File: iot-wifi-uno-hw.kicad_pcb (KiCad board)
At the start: 2 copper layers, 68.6 x 53.3 mm, 87 parts, among them CON1 BARREL_JACK, P1 CONN_01X08, P2 CONN_01X08, P3 CONN_01X06, P4 CONN_01X10, P5 CONN_01X04, Q1 MMBT8050LT1G, Q2 MMBT8050LT1G, U1 usb_mini_b, U2 MCP16311-MNY, U3 CH340G, U4 ESP-12E, U5 MCP6001R, U6 BD00GA5WEFJ, U7 IRLM6402, X1 CRYSTAL_ABM3C

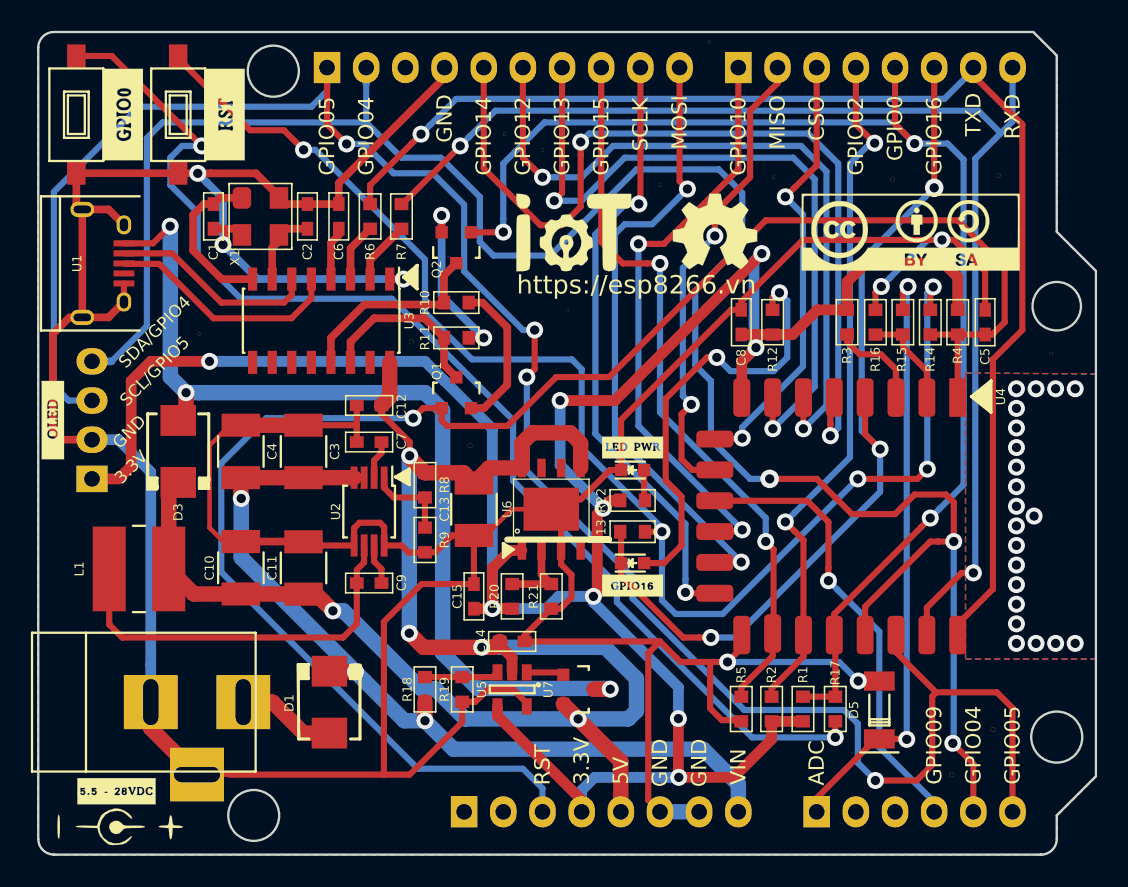
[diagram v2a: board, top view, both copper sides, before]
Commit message: Fix Zone at module wifi esp-12
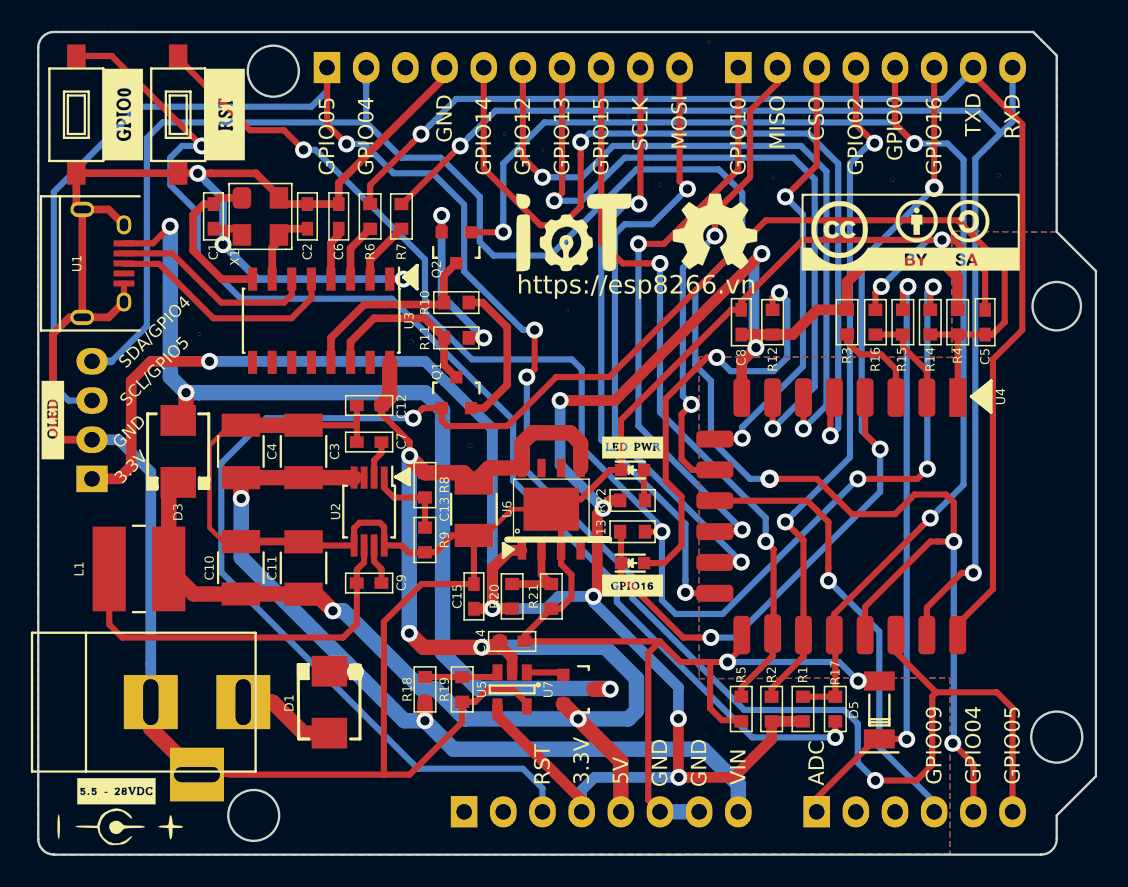
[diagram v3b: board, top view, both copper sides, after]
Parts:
- removed the REF** at (168.2, 106.8)
- removed the REF** at (174.6, 79.5)
- removed the REF** at (170.8, 103.9)
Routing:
- net (no net): vias 21 -> 0
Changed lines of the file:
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@@
   (general
     (links 164)
-    (no_connects 5)
-    (area 107.7265 55.797666 178.201339 114.382333)
+    (no_connects 16)
+    (area 107.7265 55.404 187.068335 114.382333)
     (thickness 1.6)
-    (drawings 87)
-    (tracks 850)
+    (drawings 89)
+    (tracks 829)
     (zones 0)
-    (modules 87)
+    (modules 84)
     (nets 50)
   )
@@
   )
   (module ESP8266:gnd_via (layer F.Cu)
-    (at 174.625 79.502)
-    (fp_text reference REF** (at 0.1016 0.8636) (layer F.SilkS) hide
-      (effects (font (size 0.8 0.8) (thickness 0.15)))
-    )
-    (fp_text value gnd_via (at 0 -0.5) (layer F.Fab) hide
-      (effects (font (size 1 1) (thickness 0.15)))
-    )
-    (pad GND thru_hole circle (at 0.6 0) (size 0.2 0.2) (drill 0.2) (layers *.Cu *.Mask)
-      (net 34 GND))
-  )
-  (module ESP8266:gnd_via (layer F.Cu)
     (at 141.64 66.294)
     (fp_text reference REF** (at 0.1016 0.8636) (layer F.SilkS) hide
@@
   )
   (module ESP8266:gnd_via (layer F.Cu)
-    (at 170.85 103.886)
-    (fp_text reference REF** (at 0.1016 0.8636) (layer F.SilkS) hide
-      (effects (font (size 0.8 0.8) (thickness 0.15)))
-    )
-    (fp_text value gnd_via (at 0 -0.5) (layer F.Fab) hide
-      (effects (font (size 1 1) (thickness 0.15)))
-    )
-    (pad GND thru_hole circle (at 0.6 0) (size 0.3 0.3) (drill 0.3) (layers *.Cu *.Mask)
-      (net 34 GND))
-  )
-  (module ESP8266:gnd_via (layer F.Cu)
     (at 136.941 85.471)
     (fp_text reference REF** (at 0.1016 0.8636) (layer F.SilkS) hide
@@
       (net 34 GND))
   )
-  (module ESP8266:gnd_via (layer F.Cu)
-    (at 168.183 106.807)
-    (fp_text reference REF** (at 0.1016 0.8636) (layer F.SilkS) hide
-      (effects (font (size 0.8 0.8) (thickness 0.15) italic))
-    )
-    (fp_text value gnd_via (at 0 -0.5) (layer F.Fab) hide
-      (effects (font (size 1 1) (thickness 0.15)))
-    )
-    (pad GND thru_hole circle (at 0.6 0) (size 0.3 0.3) (drill 0.3) (layers *.Cu *.Mask)
-      (net 34 GND))
-  )
   (module ESP8266:do214aa-g (layer F.Cu)
     (at 128.4224 102.108 270)
@@
       (xy -0.353299 -2.4892) (xy 0.01385 -2.4892) (xy 0.143961 -2.488787)) (layer F.SilkS) (width 0.01))
   )
+  (dimension 53.34 (width 0.25) (layer F.SilkS)
+    (gr_text "53,340 mm" (at 182.61 85.344 270) (layer F.SilkS)
+      (effects (font (size 1 1) (thickness 0.25)))
+    )
+    (feature1 (pts (xy 178.562 112.014) (xy 183.61 112.014)))
+    (feature2 (pts (xy 178.562 58.674) (xy 183.61 58.674)))
+    (crossbar (pts (xy 181.61 58.674) (xy 181.61 112.014)))
+    (arrow1a (pts (xy 181.61 112.014) (xy 181.023579 110.887496)))
+    (arrow1b (pts (xy 181.61 112.014) (xy 182.196421 110.887496)))
+    (arrow2a (pts (xy 181.61 58.674) (xy 181.023579 59.800504)))
+    (arrow2b (pts (xy 181.61 58.674) (xy 182.196421 59.800504)))
+  )
+  (dimension 68.58 (width 0.25) (layer F.SilkS)
+    (gr_text "68,580 mm" (at 143.764 56.404) (layer F.SilkS)
+      (effects (font (size 1 1) (thickness 0.25)))
+    )
+    (feature1 (pts (xy 178.054 58.42) (xy 178.054 55.404)))
+    (feature2 (pts (xy 109.474 58.42) (xy 109.474 55.404)))
+    (crossbar (pts (xy 109.474 57.404) (xy 178.054 57.404)))
+    (arrow1a (pts (xy 178.054 57.404) (xy 176.927496 57.990421)))
+    (arrow1b (pts (xy 178.054 57.404) (xy 176.927496 56.817579)))
+    (arrow2a (pts (xy 109.474 57.404) (xy 110.600504 57.990421)))
+    (arrow2b (pts (xy 109.474 57.404) (xy 110.600504 56.817579)))
+  )
   (gr_line (start 170.942 82.042) (end 170.815 82.296) (layer F.SilkS) (width 0.2))
   (gr_line (start 170.942 82.55) (end 170.942 82.042) (layer F.SilkS) (width 0.2))
@@
   (segment (start 146.558 91.567) (end 145.288 91.567) (width 0.4) (layer F.SilkS) (net 0))
   (segment (start 139.954 91.567) (end 146.558 91.567) (width 0.4) (layer F.SilkS) (net 0))
-  (via (at 174.117 90.043) (size 1.1) (drill 0.6) (layers F.Cu B.Cu) (net 0))
-  (via (at 176.784 98.298) (size 1.1) (drill 0.6) (layers F.Cu B.Cu) (net 0))
-  (via (at 175.514 98.298) (size 1.1) (drill 0.6) (layers F.Cu B.Cu) (net 0))
-  (via (at 174.244 98.298) (size 1.1) (drill 0.6) (layers F.Cu B.Cu) (net 0))
-  (via (at 172.974 98.298) (size 1.1) (drill 0.6) (layers F.Cu B.Cu) (net 0))
-  (via (at 172.974 97.028) (size 1.1) (drill 0.6) (layers F.Cu B.Cu) (net 0))
-  (via (at 176.784 81.788) (size 1.1) (drill 0.6) (layers F.Cu B.Cu) (net 0))
-  (via (at 175.514 81.788) (size 1.1) (drill 0.6) (layers F.Cu B.Cu) (net 0))
-  (via (at 174.244 81.788) (size 1.1) (drill 0.6) (layers F.Cu B.Cu) (net 0))
-  (via (at 172.974 95.758) (size 1.1) (drill 0.6) (layers F.Cu B.Cu) (net 0))
-  (via (at 172.974 94.488) (size 1.1) (drill 0.6) (layers F.Cu B.Cu) (net 0))
-  (via (at 172.974 93.218) (size 1.1) (drill 0.6) (layers F.Cu B.Cu) (net 0))
-  (via (at 172.974 91.948) (size 1.1) (drill 0.6) (layers F.Cu B.Cu) (net 0))
-  (via (at 172.974 90.678) (size 1.1) (drill 0.6) (layers F.Cu B.Cu) (net 0))
-  (via (at 172.974 89.408) (size 1.1) (drill 0.6) (layers F.Cu B.Cu) (net 0))
-  (via (at 172.974 88.138) (size 1.1) (drill 0.6) (layers F.Cu B.Cu) (net 0))
-  (via (at 172.974 86.868) (size 1.1) (drill 0.6) (layers F.Cu B.Cu) (net 0))
-  (via (at 172.974 85.598) (size 1.1) (drill 0.6) (layers F.Cu B.Cu) (net 0))
-  (via (at 172.974 84.328) (size 1.1) (drill 0.6) (layers F.Cu B.Cu) (net 0))
-  (via (at 172.974 83.058) (size 1.1) (drill 0.6) (layers F.Cu B.Cu) (net 0))
-  (via (at 172.974 81.788) (size 1.1) (drill 0.6) (layers F.Cu B.Cu) (net 0))
   (segment (start 120.904 69.812001) (end 120.294299 69.812001) (width 0.5) (layer F.Cu) (net 1))
   (segment (start 120.294299 69.812001) (end 119.5832 70.5231) (width 0.5) (layer F.Cu) (net 1))
@@
   (segment (start 155.11 93.048) (end 155.1305 93.0275) (width 0.4) (layer F.Cu) (net 26))
   (via (at 155.1305 93.0275) (size 1.1) (drill 0.6) (layers F.Cu B.Cu) (net 26))
+  (segment (start 148.491758 69.803989) (end 147.64323 69.803989) (width 0.4) (layer B.Cu) (net 27))
+  (segment (start 147.64323 69.803989) (end 146.05 71.397219) (width 0.4) (layer B.Cu) (net 27))
+  (segment (start 146.05 71.397219) (end 146.05 85.09) (width 0.4) (layer B.Cu) (net 27))
+  (segment (start 146.05 85.09) (end 151.511 90.551) (width 0.4) (layer B.Cu) (net 27))
+  (segment (start 151.511 90.551) (end 151.511 94.147472) (width 0.4) (layer B.Cu) (net 27))
+  (segment (start 151.511 94.147472) (end 151.511 94.996) (width 0.4) (layer B.Cu) (net 27))
   (segment (start 151.563 95.048) (end 151.511 94.996) (width 0.4) (layer F.Cu) (net 27))
   (segment (start 153.414 95.048) (end 151.563 95.048) (width 0.4) (layer F.Cu) (net 27))
-  (segment (start 151.511 94.147472) (end 151.511 94.996) (width 0.4) (layer B.Cu) (net 27))
-  (segment (start 151.511 90.551) (end 151.511 94.147472) (width 0.4) (layer B.Cu) (net 27))
-  (segment (start 145.669 71.778219) (end 145.669 84.709) (width 0.4) (layer B.Cu) (net 27))
-  (segment (start 145.669 84.709) (end 151.511 90.551) (width 0.4) (layer B.Cu) (net 27))
-  (segment (start 147.64323 69.803989) (end 145.669 71.778219) (width 0.4) (layer B.Cu) (net 27))
-  (segment (start 148.491758 69.803989) (end 147.64323 69.803989) (width 0.4) (layer B.Cu) (net 27))
   (via (at 151.511 94.996) (size 1.1) (drill 0.6) (layers F.Cu B.Cu) (net 27))
   (segment (start 148.59 69.705747) (end 148.491758 69.803989) (width 0.4) (layer F.Cu) (net 27))
@@
     (polygon
       (pts
-        (xy 110.2868 58.674) (xy 174.0916 58.674) (xy 175.6156 60.198) (xy 175.6156 71.628) (xy 178.1556 74.168)
-        (xy 178.1556 80.8228) (xy 169.672 80.772) (xy 169.672 99.314) (xy 178.1556 99.314) (xy 178.1556 106.934)
-        (xy 175.6156 109.474) (xy 175.6156 111.2012) (xy 175.26 111.76) (xy 174.8028 112.014) (xy 174.3964 112.014)
-        (xy 110.49 112.014) (xy 109.982 111.8108) (xy 109.6264 111.4552) (xy 109.5248 110.998) (xy 109.5248 59.436)
-        (xy 109.728 59.0804) (xy 109.982 58.8264)
+        (xy 110.4392 58.6232) (xy 174.0916 58.674) (xy 175.6156 60.198) (xy 175.5648 71.628) (xy 168.8084 71.5772)
+        (xy 168.8084 79.756) (xy 152.4 79.7052) (xy 152.4 100.584) (xy 168.656 100.5332) (xy 168.656 111.9632)
+        (xy 110.5916 112.014) (xy 110.0328 111.8616) (xy 109.6264 111.4552) (xy 109.5248 111.0996) (xy 109.5248 59.4868)
+        (xy 109.7788 58.9788) (xy 110.1852 58.7248)
       )
     )
@@
     (polygon
       (pts
-        (xy 110.2868 58.674) (xy 174.0916 58.674) (xy 175.6156 60.198) (xy 175.6156 71.628) (xy 178.1556 74.168)
-        (xy 178.1556 80.8228) (xy 169.672 80.772) (xy 169.672 99.314) (xy 178.1556 99.314) (xy 178.1556 106.8832)
-        (xy 175.5648 109.474) (xy 175.6156 111.0996) (xy 175.4632 111.506) (xy 175.26 111.76) (xy 174.9044 111.9632)
-        (xy 174.5488 112.014) (xy 110.49 112.014) (xy 109.982 111.8108) (xy 109.6264 111.4552) (xy 109.5248 110.998)
-        (xy 109.5248 59.4868) (xy 109.6772 59.0804) (xy 109.9312 58.8264)
+        (xy 110.4392 58.6232) (xy 174.0916 58.674) (xy 175.6156 60.198) (xy 175.5648 71.628) (xy 168.7576 71.5772)
+        (xy 168.8084 79.756) (xy 152.4 79.7052) (xy 152.4 99.314) (xy 152.4 100.584) (xy 168.656 100.5332)
+        (xy 168.656 112.014) (xy 110.5916 112.014) (xy 109.982 111.8108) (xy 109.5756 111.3028) (xy 109.5248 110.8456)
+        (xy 109.5248 59.4868) (xy 109.728 59.0296) (xy 110.1344 58.7248)
       )
     )

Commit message: fix transistor to 1b 2e 3c on datasheet MMBT8050
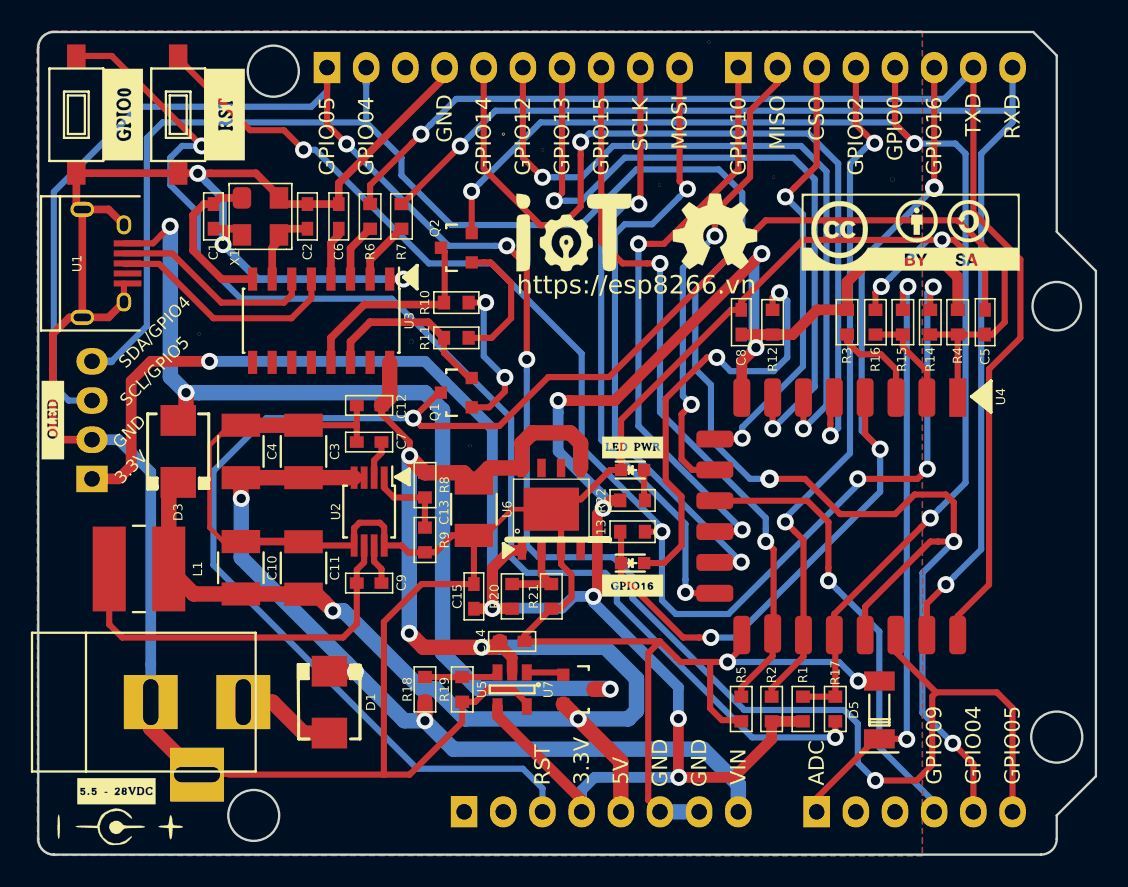
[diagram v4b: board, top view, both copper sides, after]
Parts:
- removed the REF** at (171.2, 67.9)
- C5: value 470pF -> 100nF
- Q1, Q2: value MMBT8050LT1G -> Q_NPN_BEC
- R1, R2, R3, R4, R5: value 12k -> 10k
- REF**: moved to B.Cu
- U6: footprint HTSOP-J8 -> ESP8266:HTSOP-J8
- moved REF** 4.42 mm to (143.2, 72.3)
- moved REF** 0.09 mm to (139.1, 65.3)
- turned Q1 to 90 degrees
- turned Q2 to 90 degrees
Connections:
- Q1 pad 1: REST -> Net-(Q1-Pad1)
- Q1 pad 3: Net-(Q1-Pad3) -> REST
- Q2 pad 1: GPIO0 -> Net-(Q2-Pad1)
- Q2 pad 2: Net-(Q2-Pad2) -> GPIO0
- R10 pad 2: Net-(Q1-Pad2) -> Net-(Q1-Pad1)
- R11 pad 1: Net-(Q1-Pad3) -> Net-(Q1-Pad2)
- R11 pad 2: Net-(Q2-Pad2) -> Net-(Q2-Pad1)
- U3 pad 14: Net-(Q1-Pad3) -> Net-(Q1-Pad2)
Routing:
- net Net-(Q1-Pad3): track 11.4 -> 0.00 mm
- net Net-(Q2-Pad2): track 11.1 -> 0.00 mm, vias 2 -> 0
- net Net-(Q1-Pad1): track 0.00 -> 10.1 mm, vias 0 -> 2
- net Net-(Q2-Pad1): track 0.00 -> 8.68 mm
- net Net-(GPIO1-Pad1): track 78.3 -> 81.3 mm
- net GPIO5: track 131.7 -> 133.7 mm
- net REST: track 108.7 -> 110.7 mm
- net Net-(Q1-Pad2): track 9.89 -> 11.8 mm
- net Net-(R13-Pad2): track 89.9 -> 88.7 mm
- net GPIO4: track 133.0 -> 131.9 mm
- net GPIO0: track 84.4 -> 83.7 mm
- net Net-(Q2-Pad3): track 12.8 -> 13.4 mm
